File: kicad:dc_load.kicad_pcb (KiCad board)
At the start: 2 copper layers, 182.8 x 78.4 mm, 57 parts, among them J2 LCD socket pin, J3 Conn_01x02, J4 Encoder, J5 GPIO expander, J6 ADS1115 ADC, J7 +, J8 -, Q2 IRLZ44N, Q3 IRLZ44N, U2 L7805, U3 ESP32-C3, U4 TL431LP, U5 MCP4725, U6 LM324

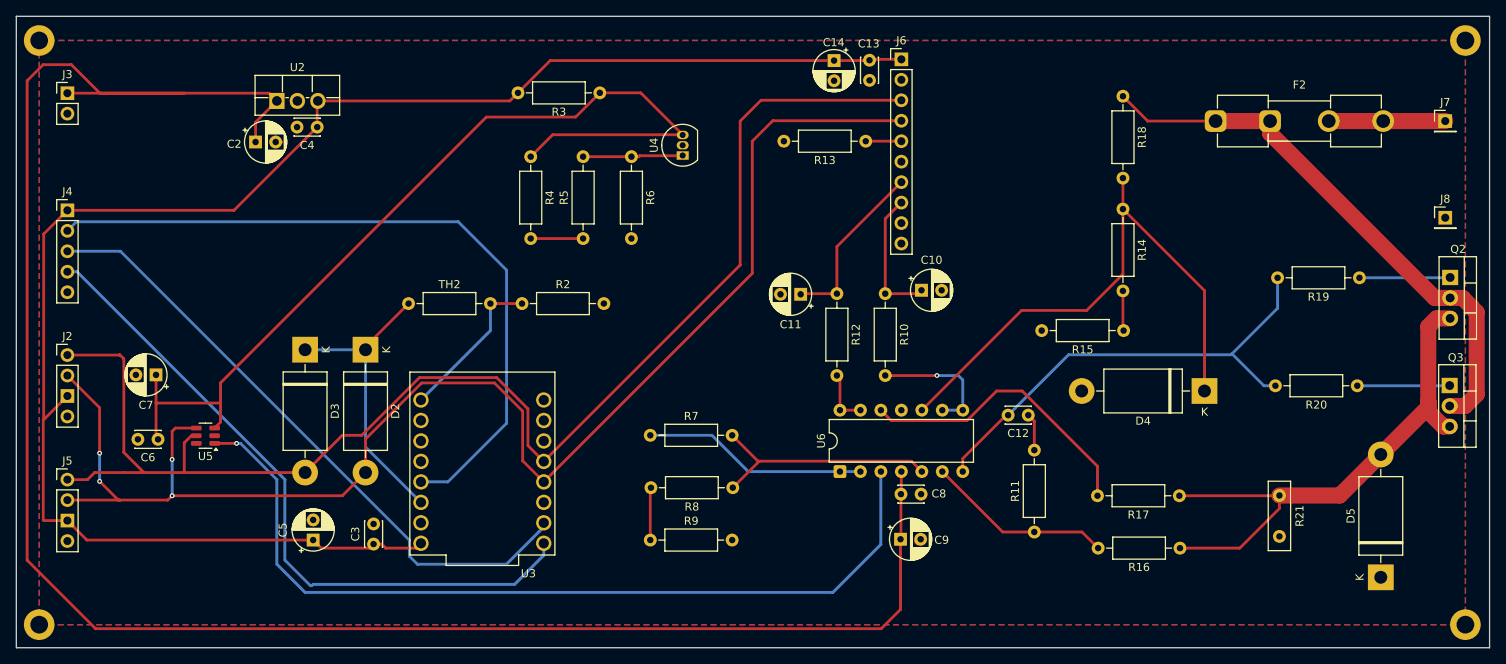
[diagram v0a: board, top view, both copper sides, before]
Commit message: Resized PCB and added some caps
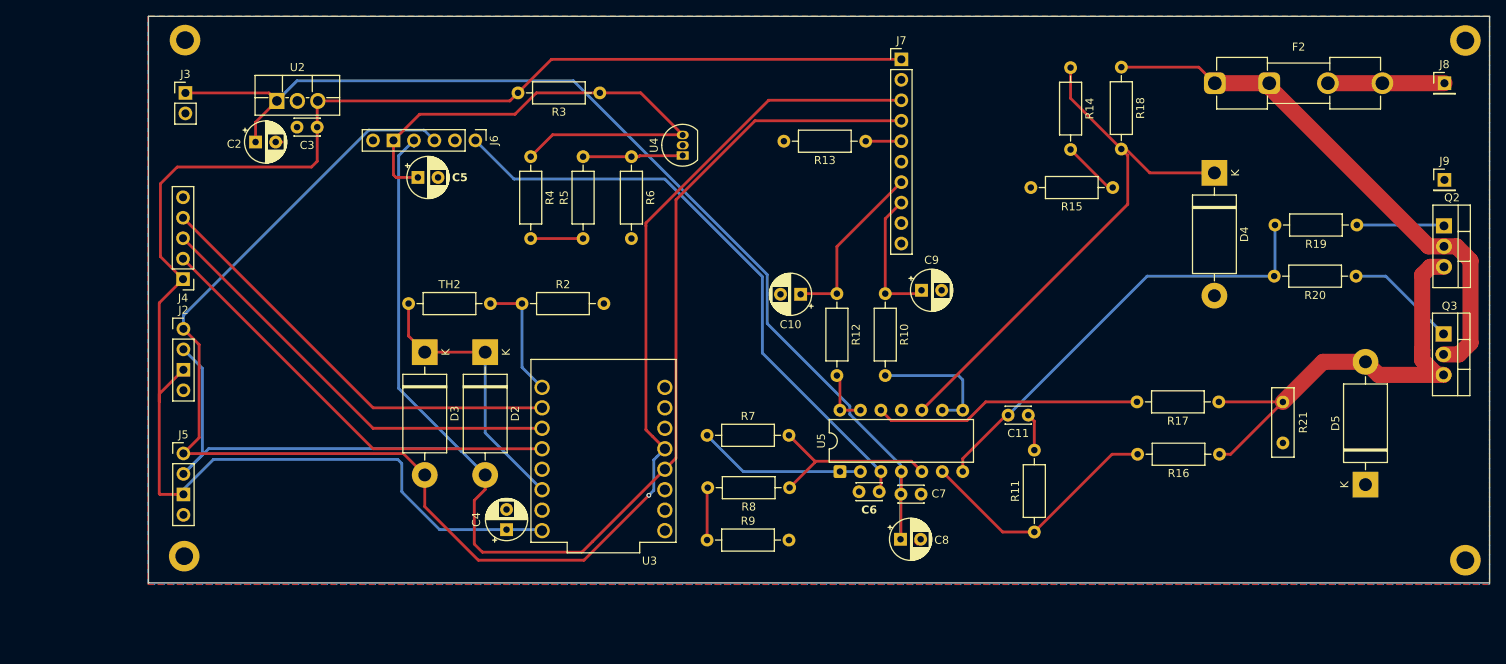
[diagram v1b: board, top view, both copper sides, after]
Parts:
- removed C13: 0.1u, Capacitor_THT:C_Disc_D3.0mm_W2.0mm_P2.50mm
- removed C14: 10u, Capacitor_THT:CP_Radial_D5.0mm_P2.50mm
- removed the C3 at (86.0, 82.0)
- removed the C7 at (59.0, 61.0)
- removed the U5 at (65.1, 68.5)
- added C4: 220u, Capacitor_THT:CP_Radial_D5.0mm_P2.50mm, F.Cu at (102.5, 80.2)
- added J6: MCP4725, Connector_PinHeader_2.54mm:PinHeader_1x06_P2.54mm_Vertical, F.Cu at (98.6, 31.9)
- moved C6 89.7 mm to (148.8, 75.5)
- moved C5 46.8 mm to (91.5, 36.5), turned to 0 degrees
- moved D4 27.1 mm to (190.3, 35.9), turned to -90 degrees
- moved REF04 19.9 mm to (62.5, 83.5)
- moved R14 18.7 mm to (172.5, 22.9)
- moved REF01 18.1 mm to (62.6, 19.4)
- moved R15 17.8 mm to (177.7, 37.8)
- moved J4 16.7 mm to (62.4, 49.1), turned to 180 degrees
- moved U3 15.1 mm to (114.5, 70.4)
- moved D2 14.9 mm to (99.8, 58.2)
- moved D3 14.9 mm to (92.3, 58.2)
- moved J2 14.8 mm to (62.4, 55.3)
- moved J5 14.8 mm to (62.4, 70.8)
- moved J3 14.7 mm to (62.6, 26.0)
- moved R20 13.6 mm to (207.9, 48.8)
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- renumbered C11 to C10, C12 to C11, C4 to C3, C8 to C7, C9 to C8, C10 to C9, J6 to J7, J7 to J8, J8 to J9, U6 to U5
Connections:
- C5 pad 1: +5V -> /4.096V
- C6 pad 1: /4.096V -> Net-(J6-Pin_1)
- REF01 pad 1: (no net) -> GND
- REF02 pad 1: (no net) -> GND
- REF03 pad 1: (no net) -> GND
- REF04 pad 1: (no net) -> GND
- U3 pad 1: unconnected-(U3-GPIO1-Pad1) -> /S1
- U3 pad 2: unconnected-(U3-GPIO2-Pad2) -> /S2
- U3 pad 3: unconnected-(U3-GPIO3-Pad3) -> /BTN
- U3 pad 4: /BTN -> unconnected-(U3-GPIO4-Pad4)
- U3 pad 5: /S1 -> unconnected-(U3-GPIO5-Pad5)
- U3 pad 6: /S2 -> unconnected-(U3-GPIO6-Pad6)
- U5 pad 3: Net-(U5-VOUT) -> Net-(J6-Pin_1)
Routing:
- net Net-(U5-VOUT): track 108.0 -> 0.00 mm, vias 1 -> 0
- net +12V: track 243.9 -> 138.0 mm
- net Net-(J6-Pin_1): track 0.00 -> 75.5 mm
- net /4.096V: track 115.6 -> 67.2 mm
- net /BTN: track 90.1 -> 54.3 mm
- net /SCL: track 172.7 -> 203.5 mm, vias 0 -> 1
- net /S1: track 84.2 -> 54.3 mm
- net /SDA: track 178.2 -> 204.4 mm, vias 4 -> 0
- net /S2: track 78.8 -> 54.3 mm
- net Net-(D5-A): track 69.3 -> 59.0 mm
- net Net-(U5B--): track 23.3 -> 31.3 mm
- net Net-(U5B-+): track 30.1 -> 22.9 mm
- net Net-(U5A--): track 27.9 -> 20.9 mm
- net Net-(U3-GPIO0): track 19.5 -> 15.4 mm
- net Net-(U5D-+): track 36.5 -> 33.3 mm
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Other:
- board size 182.8 x 78.4 mm -> 166.4 x 70.3 mm
